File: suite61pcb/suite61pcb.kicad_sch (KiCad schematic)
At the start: 96 parts, among them J1 Battery JST, J2 OLED, J3 FFC_Receiver, SW1 MX_SW_HS, SW10 MX_SW_HS, SW11 MX_SW_HS, SW12 MX_SW_HS, SW13 MX_SW, SW14 MX_SW, SW15 MX_SW_HS, SW16 MX_SW_HS, SW17 MX_SW_HS, SW18 MX_SW_HS, SW19 MX_SW_HS, SW2 MX_SW_HS, SW20 Reset_Button, SW21 MX_SW, SW22 MX_SW, SW23 MX_SW_HS, SW24 MX_SW_HS, SW25 MX_SW_HS, SW26 MX_SW_HS, SW27 MX_SW_HS, SW28 MX_SW_HS, SW29 MX_SW_HS, SW3 MX_SW_HS, SW30 MX_SW_HS, SW31 MX_SW_HS, SW32 MX_SW_HS, SW33 MX_SW_HS, SW34 MX_SW_HS, SW35 MX_SW_HS, SW36 MX_SW_HS, SW37 RotaryEncoder_Switch, SW4 MX_SW_HS, SW5 MX_SW_HS, SW6 MX_SW_HS, SW7 MX_SW_HS, SW8 MX_SW_HS, SW9 MX_SW_HS, U1 nice_nano

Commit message: update pcb
finished routing switch matrix, only need to do joystick & LEDs
figure out how battery is gonna fit to keep underglow unobstructed
decide on magnetic connector
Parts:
- J2: footprint Connector_PinHeader_2.00mm:PinHeader_1x04_P2.00mm_Vertical -> SofleKeyboard-footprint:OLED_4Pin
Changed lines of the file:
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@@
     (property "Reference" "J2" (id 0) (at 238.76 114.3 0))
     (property "Value" "OLED" (id 1) (at 238.76 116.84 0))
-    (property "Footprint" "Connector_PinHeader_2.00mm:PinHeader_1x04_P2.00mm_Vertical" (id 2) (at 238.76 125.73 0)
+    (property "Footprint" "SofleKeyboard-footprint:OLED_4Pin" (id 2) (at 238.76 125.73 0)
       (effects (font (size 1.27 1.27)) hide)
     )
@@
     )
     (path "/f88f3bce-421d-4ea6-bc4e-2ce69437148b"
-      (reference "J2") (unit 1) (value "OLED") (footprint "Connector_PinHeader_2.00mm:PinHeader_1x04_P2.00mm_Vertical")
+      (reference "J2") (unit 1) (value "OLED") (footprint "SofleKeyboard-footprint:OLED_4Pin")
     )
     (path "/8ef6be0b-6e32-4acb-b9a5-f9b261e41966"

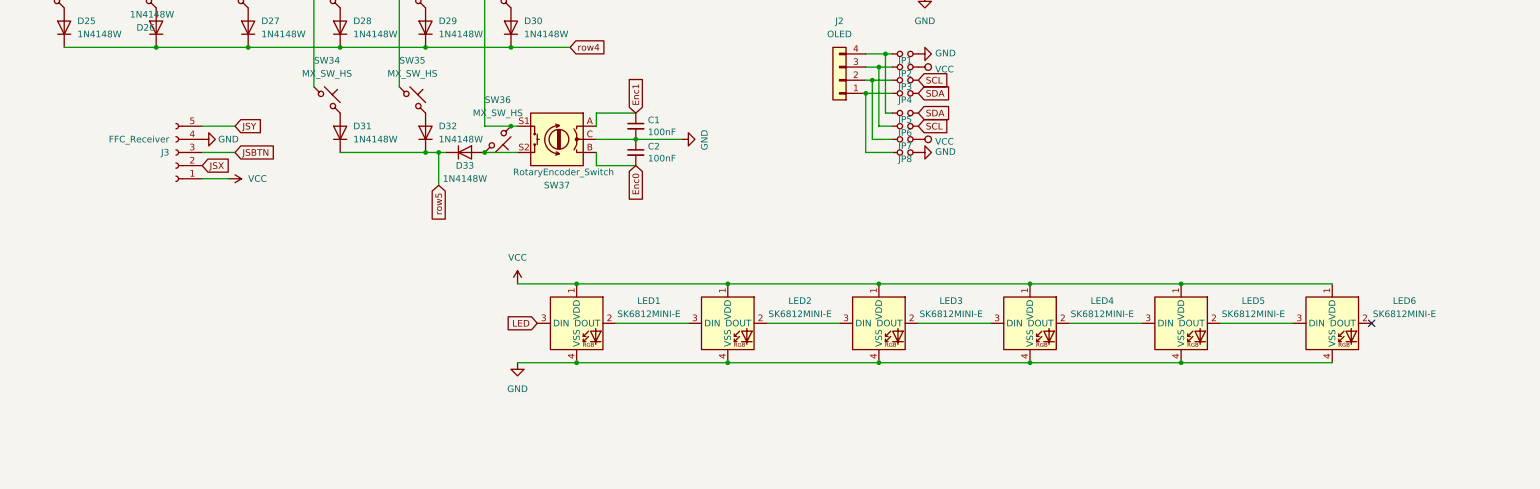
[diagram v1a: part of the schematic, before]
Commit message: finished routing pcb, look into possible trrs + magnetic connection between halves
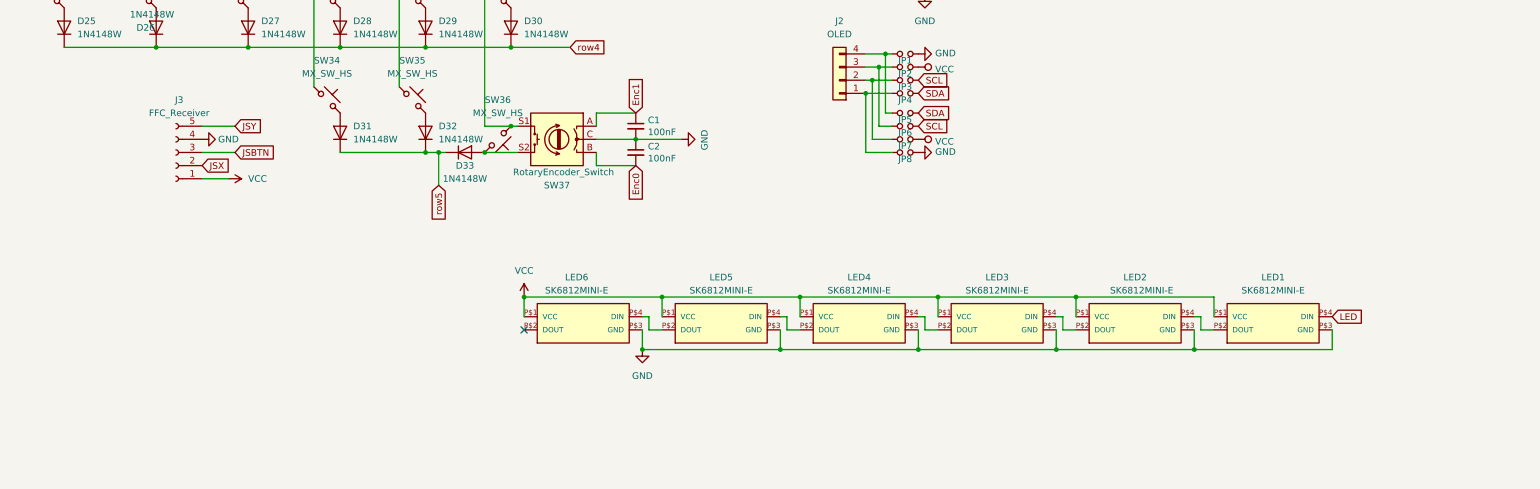
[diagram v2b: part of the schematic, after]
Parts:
- LED1, LED2, LED3, LED4, LED5, LED6: footprint LED_SMD:LED_SK6812MINI_PLCC4_3.5x3.5mm_P1.75mm -> marbastlib-various:LED_6028R; symbol marbastlib-various:SK6812MINI-E -> SK6812MINI-E:SK6812MINI-E
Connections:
- net GND: now also LED1.P$3 (GND), LED2.P$3 (GND), LED3.P$3 (GND), LED4.P$3 (GND), LED5.P$3 (GND), LED6.P$3 (GND); no longer LED1.4 (VSS), LED2.4 (VSS), LED3.4 (VSS), LED4.4 (VSS), LED5.4 (VSS), LED6.4 (VSS)
- net LED: now also LED1.P$4 (DIN); no longer LED1.3 (DIN)
- net VCC: now also LED1.P$1 (VCC), LED2.P$1 (VCC), LED3.P$1 (VCC), LED4.P$1 (VCC), LED5.P$1 (VCC), LED6.P$1 (VCC); no longer LED1.1 (VDD), LED2.1 (VDD), LED3.1 (VDD), LED4.1 (VDD), LED5.1 (VDD), LED6.1 (VDD)
- new net: LED2.P$2 (DOUT), LED3.P$4 (DIN)
- new net: LED1.P$2 (DOUT), LED2.P$4 (DIN)
- new net: LED5.P$2 (DOUT), LED6.P$4 (DIN)
- new net: LED4.P$2 (DOUT), LED5.P$4 (DIN)
- new net: LED3.P$2 (DOUT), LED4.P$4 (DIN)

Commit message: routing & edge design
finished routing pcb, added LED off switch
drew edge design in illustrator subject to change
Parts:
- removed J2: OLED, SofleKeyboard-footprint:OLED_4Pin, symbol Connector_Generic:Conn_01x04
- added Display1: nice!view, nice_view:nice_view, symbol nice_view:nice!view
- added J3: FFC_Receiver, LIB_503480-0500:5034800500, symbol Connector:Conn_01x05_Female
- added JP1, JP10: Jumper_NO_Small, suite61:jumper, symbol SofleKeyboard-rescue:Jumper_NO_Small-Device
- added S2: MSK12C02, LIB_MSK12C02:MSK12C02, symbol MSK12C02:MSK12C02
- J1: footprint suite61:JST_S2B-PH-SM4-TB -> suite61:JST_SH_SM02B-SRSS-TB_1x02-1MP_P1.00mm_Horizontal
- renumbered J3 to J2, JP1 to JP2, JP2 to JP3, JP3 to JP4, JP4 to JP5, JP5 to JP6, JP6 to JP7, JP7 to JP8, JP8 to JP9
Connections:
- net GND: now also J3.4 (Pin_4), S2.MP1, S2.MP2, S2.MP3, S2.MP4
- net JSBTN: now also J3.3 (Pin_3)
- net JSX: now also J2.5 (Pin_5), U1.19 (AIN5/P0.29), J3.5 (Pin_5); no longer J2.2 (Pin_2), U1.20 (AIN7/P0.31)
- net JSY: now also J2.2 (Pin_2), U1.20 (AIN7/P0.31), J3.2 (Pin_2); no longer J2.5 (Pin_5), U1.19 (AIN5/P0.29)
- net VCC: now also J3.1 (Pin_1), S2.B1 (COM); no longer LED1.P$1 (VCC), LED2.P$1 (VCC), LED3.P$1 (VCC), LED4.P$1 (VCC), LED5.P$1 (VCC), LED6.P$1 (VCC)
- net at JP2.1: now also JP7.1, Display1.4 (GND); no longer JP6.1
- net at JP5.1: now also Display1.1 (MOSI), JP10.1; no longer JP9.1
- net at JP4.1: now also JP9.1, Display1.2 (SCK); no longer JP8.1
- net at JP3.1: now also JP8.1, Display1.3 (VCC); no longer JP7.1
- net DATA renamed DISPLAY
- net DISPLAY: now also JP1.2, JP10.2
- new net: Display1.5 (CS), JP1.1, JP6.1
- new net LEDPWR: LED1.P$1 (VCC), LED2.P$1 (VCC), LED3.P$1 (VCC), LED4.P$1 (VCC), LED5.P$1 (VCC), LED6.P$1 (VCC), S2.C1 (NO)
- no-connect marks 2 -> 1
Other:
- moved on the sheet: JP2, JP3, JP4, JP5, JP6, JP7, JP8, JP9
